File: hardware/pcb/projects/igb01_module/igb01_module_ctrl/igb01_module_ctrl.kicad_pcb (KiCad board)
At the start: 2 copper layers, 131 x 111 mm, 300 parts, among them J1 ST_JACK_MIDI_OUT, J10 JACK_MAIN_L_OUT, J11 JACK_MAIN_R_OUT, J12 ST_JACK_MIDI_IN, J13 JACK_RST_OUT, J14 JACK_CV_Y_IN, J15 JACK_CV_E_OUT, J16 JACK_CV_F_OUT, J17 JACK_CV_G_OUT, J18 JACK_CV_H_OUT, J19 JACK_RTN_L_IN, J2 JACK_CLK_OUT, J20 JACK_RTN_R_IN, J21 JACK_SND_L_OUT, J22 JACK_SND_R_OUT, J23 TYPE_SELECT, J24 LEFT_CON, J25 RIGHT_CON, J26 TYPE_SELECT, J27 SWD_CON, J28 DISP_CON1, J29 Micro_SD_Card, J3 JACK_CV_X_IN, J30 Conn_01x03, J31 Conn_01x03, J32 Conn_01x03, J33 POWER_CON, J4 JACK_CV_A_OUT, J5 JACK_CV_B_OUT, J6 JACK_CV_C_OUT, J7 JACK_CV_D_OUT, J8 JACK_EXT_L_IN, J9 JACK_EXT_R_IN, SW1 SW_Push_45deg, SW10 SW_Push_45deg, SW11 SW_Push_45deg, SW12 SW_Push_45deg, SW13 SW_Push_45deg, SW14 SW_Push_45deg, SW15 SW_Push_45deg, SW16 SW_Push_45deg, SW17 SW_Push_45deg, SW18 SW_Push_45deg, SW19 SW_Push_45deg, SW2 SW_Push_45deg, SW20 SW_Push_45deg, SW21 SW_Push_45deg, SW22 SW_Push_45deg, SW23 SW_Push_45deg, SW24 SW_Push_45deg, SW25 SW_Push_45deg, SW26 SW_Push_45deg, SW27 SW_Push_45deg, SW28 SW_Push_45deg, SW29 SW_Push_45deg, SW3 SW_Push_45deg, SW30 SW_Push_45deg, SW31 SW_Push_45deg, SW32 SW_Push_45deg, SW33 SW_Push_45deg, SW34 SW_Push_45deg, SW35 SW_Push_45deg, SW36 SW_Push_45deg, SW4 SW_Push_45deg, SW5 SW_Push_45deg, SW6 SW_Push_45deg, SW7 SW_Push_45deg, SW8 SW_Push_45deg, SW9 SW_Push_45deg, U1 TL074, U10 STM32G431RBTx, U11 TL074, U12 R-78B5.0-2.0, U13 LDK320-3.3V, U14 LDK320-3.3V, U15 LM4040DBZ-10, U2 TL074, U3 74AHCT1G125, U4 TLP2361, U5 74AHCT1G125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

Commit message: update igb01 module control board
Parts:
- removed the C41 at (291.0, 124.2)
- removed the C42 at (291.0, 129.2)
- removed the C43 at (291.0, 126.7)
- removed the C44 at (291.0, 131.7)
- removed the C45 at (291.0, 134.3)
- removed the C46 at (295.0, 101.6)
- removed the C47 at (291.0, 136.8)
- removed the C48 at (295.0, 104.1)
- removed the R19 at (299.0, 134.3)
- removed the R29 at (303.0, 121.7)
- removed the R32 at (303.0, 129.2)
- removed the R48 at (307.0, 106.6)
- added C26: 10u, Capacitor_SMD:C_0805_2012Metric, B.Cu at (115.5, 113.1)
- C1, C10, C11, C12, C13, C14, C15, C16, C17, C18, C19, C2, C20, C21, C22, C23, C24, C25, C3, C4, C5, C6, C7, C8, C9, FB1, FB2, FB3, J23, J26, J27, JP1, R11, R12, R13, R14, R15, R16, R17, R18, U1, U11, U12, U13, U14, U15, U2, U3, U4, U5, U6, U7, U8, U9, Y1: moved to B.Cu
- C27: renamed from C26; moved to B.Cu
- C28: renamed from C27; footprint Capacitor_SMD:C_1206_3216Metric -> Capacitor_SMD:C_0805_2012Metric; moved to B.Cu
- C29: renamed from C28; moved to B.Cu
- C30: renamed from C29; moved to B.Cu
- C31: renamed from C30; moved to B.Cu
- C32: renamed from C31; moved to B.Cu
- C33: renamed from C32; moved to B.Cu
- C34: renamed from C33; moved to B.Cu
- C35: renamed from C34; moved to B.Cu
- C36: renamed from C35; moved to B.Cu
- C37: renamed from C36; moved to B.Cu
- C38: renamed from C37; moved to B.Cu
- C39: renamed from C38; moved to B.Cu
- C40: renamed from C39; moved to B.Cu
- C41: renamed from C40; moved to B.Cu
- C42: renamed from C49; moved to B.Cu
- C43: renamed from C50; moved to B.Cu
- C44: renamed from C51; moved to B.Cu
- C45: renamed from C52; moved to B.Cu
- C46: renamed from C53; moved to B.Cu
- C47: renamed from C54; moved to B.Cu
- C48: renamed from C55; moved to B.Cu
- C49: renamed from C56; moved to B.Cu
- C50: renamed from C57; moved to B.Cu
- C51: renamed from C58; value 47u -> 100u; moved to B.Cu
- C52: renamed from C59; moved to B.Cu
- C53: renamed from C60; moved to B.Cu
- C54: renamed from C61; moved to B.Cu
- C55: renamed from C62; moved to B.Cu
- C56: renamed from C63; moved to B.Cu
- C57: renamed from C64; moved to B.Cu
- C58: renamed from C65; moved to B.Cu
- D1: footprint Diode_SMD:D_SOD-323_HandSoldering -> custom:SOD-123; moved to B.Cu
- D10, D11, D12, D13, D14, D15, D16, D17, D18, D19, D2, D20, D21, D22, D23, D24, D25, D26, D27, D28, D29, D3, D30, D31, D32, D33, D34, D35, D36, D37, D38, D39, D4, D40, D41, D5, D6, D7, D8, D9: footprint Diode_SMD:D_SOD-323_HandSoldering -> Diode_SMD:D_SOD-523; moved to B.Cu
- D42, D43: footprint Diode_SMD:D_SOD-123F -> custom:SOD-123; moved to B.Cu
- R1, R10, R5, R6: footprint Resistor_SMD:R_0603_1608Metric -> Resistor_SMD:R_1206_3216Metric; moved to B.Cu
- R19: renamed from R20; moved to B.Cu
- R2, R3, R4, R7, R8, R9: footprint Resistor_SMD:R_0603_1608Metric -> Resistor_SMD:R_0805_2012Metric; moved to B.Cu
- R20: renamed from R21; moved to B.Cu
- R21: renamed from R22; moved to B.Cu
- R22: renamed from R23; moved to B.Cu
- R23: renamed from R24; moved to B.Cu
- R24: renamed from R25; moved to B.Cu
- R25: renamed from R26; moved to B.Cu
- R26: renamed from R27; moved to B.Cu
- R27: renamed from R28; moved to B.Cu
- R28: renamed from R30; moved to B.Cu
- R29: renamed from R31; moved to B.Cu
- R30: renamed from R33; footprint Resistor_SMD:R_0402_1005Metric -> Resistor_SMD:R_0603_1608Metric; moved to B.Cu
- R31: renamed from R34; moved to B.Cu
- R32: renamed from R35; footprint Resistor_SMD:R_0402_1005Metric -> Resistor_SMD:R_0603_1608Metric; moved to B.Cu
- R33: renamed from R36; value 100k -> 200k; moved to B.Cu
- R34: renamed from R37; moved to B.Cu
- R35: renamed from R38; moved to B.Cu
- R36: renamed from R39; footprint Resistor_SMD:R_0402_1005Metric -> Resistor_SMD:R_0603_1608Metric; moved to B.Cu
- R37: renamed from R40; footprint Resistor_SMD:R_0402_1005Metric -> Resistor_SMD:R_0603_1608Metric; moved to B.Cu
- R38: renamed from R41; footprint Resistor_SMD:R_0402_1005Metric -> Resistor_SMD:R_0603_1608Metric; moved to B.Cu
- R39: renamed from R42; footprint Resistor_SMD:R_0402_1005Metric -> Resistor_SMD:R_0603_1608Metric; moved to B.Cu
- R40: renamed from R43; moved to B.Cu
- R41: renamed from R44; footprint Resistor_SMD:R_0402_1005Metric -> Resistor_SMD:R_0603_1608Metric; moved to B.Cu
- R42: renamed from R45; footprint Resistor_SMD:R_0402_1005Metric -> Resistor_SMD:R_0603_1608Metric; moved to B.Cu
- R43: renamed from R46; footprint Resistor_SMD:R_0402_1005Metric -> Resistor_SMD:R_0805_2012Metric; moved to B.Cu
- R44: renamed from R47; footprint Resistor_SMD:R_0402_1005Metric -> Resistor_SMD:R_0805_2012Metric; moved to B.Cu
- R45: renamed from R49; footprint Resistor_SMD:R_0402_1005Metric -> Resistor_SMD:R_0603_1608Metric; moved to B.Cu
- R46: renamed from R50; moved to B.Cu
- R47: renamed from R51; value 100k -> 200k; moved to B.Cu
- R48: renamed from R52; moved to B.Cu
- R49: renamed from R53; moved to B.Cu
- R50: renamed from R54; moved to B.Cu
- R51: renamed from R55; footprint Resistor_SMD:R_0402_1005Metric -> Resistor_SMD:R_0603_1608Metric; moved to B.Cu
- R52: renamed from R56; footprint Resistor_SMD:R_0402_1005Metric -> Resistor_SMD:R_0603_1608Metric; moved to B.Cu
- R53: renamed from R57; footprint Resistor_SMD:R_0402_1005Metric -> Resistor_SMD:R_0603_1608Metric; moved to B.Cu
- R54: renamed from R58; footprint Resistor_SMD:R_0402_1005Metric -> Resistor_SMD:R_0603_1608Metric; moved to B.Cu
- R55: renamed from R59; footprint Resistor_SMD:R_0402_1005Metric -> Resistor_SMD:R_0603_1608Metric; moved to B.Cu
- R56: renamed from R60; footprint Resistor_SMD:R_0402_1005Metric -> Resistor_SMD:R_0603_1608Metric; moved to B.Cu
- R57: renamed from R61; footprint Resistor_SMD:R_0402_1005Metric -> Resistor_SMD:R_0805_2012Metric; moved to B.Cu
- R58: renamed from R62; footprint Resistor_SMD:R_0402_1005Metric -> Resistor_SMD:R_0805_2012Metric; moved to B.Cu
- R59: renamed from R63; footprint Resistor_SMD:R_0402_1005Metric -> Resistor_SMD:R_0603_1608Metric; moved to B.Cu
- R60: renamed from R64; footprint Resistor_SMD:R_0402_1005Metric -> Resistor_SMD:R_0603_1608Metric; moved to B.Cu
- R61: renamed from R65; footprint Resistor_SMD:R_0402_1005Metric -> Resistor_SMD:R_0603_1608Metric; moved to B.Cu
- R62: renamed from R66; footprint Resistor_SMD:R_0402_1005Metric -> Resistor_SMD:R_0603_1608Metric; moved to B.Cu
- R63: renamed from R67; moved to B.Cu
- R64: renamed from R68; moved to B.Cu
- R65: renamed from R69; moved to B.Cu
- R66: renamed from R70; moved to B.Cu
- R67: renamed from R71; moved to B.Cu
- R68: renamed from R72; footprint Resistor_SMD:R_0402_1005Metric -> Resistor_SMD:R_0603_1608Metric; moved to B.Cu
- R69: renamed from R73; footprint Resistor_SMD:R_0402_1005Metric -> Resistor_SMD:R_0603_1608Metric; moved to B.Cu
- R70: renamed from R74; footprint Resistor_SMD:R_0402_1005Metric -> Resistor_SMD:R_0805_2012Metric; moved to B.Cu
- R71: renamed from R75; footprint Resistor_SMD:R_0402_1005Metric -> Resistor_SMD:R_0805_2012Metric; moved to B.Cu
- R72: renamed from R76; footprint Resistor_SMD:R_0402_1005Metric -> Resistor_SMD:R_0603_1608Metric; moved to B.Cu
- R73: renamed from R77; footprint Resistor_SMD:R_0402_1005Metric -> Resistor_SMD:R_0603_1608Metric; moved to B.Cu
- R74: renamed from R78; footprint Resistor_SMD:R_0402_1005Metric -> Resistor_SMD:R_0603_1608Metric; moved to B.Cu
- R75: renamed from R79; footprint Resistor_SMD:R_0402_1005Metric -> Resistor_SMD:R_0603_1608Metric; moved to B.Cu
- R76: renamed from R80; moved to B.Cu
- R77: renamed from R81; moved to B.Cu
- R78: renamed from R82; moved to B.Cu
- R79: renamed from R83; moved to B.Cu
- R80: renamed from R84; footprint Resistor_SMD:R_0402_1005Metric -> Resistor_SMD:R_0603_1608Metric; moved to B.Cu
- R81: renamed from R85; footprint Resistor_SMD:R_0402_1005Metric -> Resistor_SMD:R_0603_1608Metric; moved to B.Cu
- R82: renamed from R86; moved to B.Cu
- R83: renamed from R87; footprint Resistor_SMD:R_0402_1005Metric -> Resistor_SMD:R_0805_2012Metric; moved to B.Cu
- R84: renamed from R88; footprint Resistor_SMD:R_0402_1005Metric -> Resistor_SMD:R_0805_2012Metric; moved to B.Cu
- R85: renamed from R89; moved to B.Cu
- R86: renamed from R90; moved to B.Cu
- R87: renamed from R91; moved to B.Cu
- R88: renamed from R92; moved to B.Cu
- moved J31 273.0 mm to (65.5, 155.0)
- moved FB2 267.4 mm to (60.2, 130.8)
- moved FB3 256.5 mm to (66.3, 112.0)
- moved FB1 255.0 mm to (66.3, 96.0)
- moved R10 250.8 mm to (52.5, 65.6), turned to -90 degrees
- moved U12 249.3 mm to (66.6, 129.4)
- moved R5 248.4 mm to (58.7, 60.3), turned to -90 degrees
- moved R1 247.7 mm to (58.7, 52.3), turned to -90 degrees
- moved D28 247.3 mm to (63.2, 82.0), turned to -90 degrees
- moved D32 246.8 mm to (57.5, 134.3)
- moved D29 246.6 mm to (61.2, 96.0), turned to -90 degrees
- moved D33 246.4 mm to (57.5, 148.3)
- moved D30 244.9 mm to (61.2, 110.0), turned to -90 degrees
- moved U4 244.8 mm to (71.5, 87.3), turned to -90 degrees
- moved D43 244.4 mm to (71.0, 112.9)
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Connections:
- R37 pad 2: /CV_A_OUT -> /CV_B_OUT
- R39 pad 2: /CV_B_OUT -> /CV_F_OUT
- R43 pad 2: /CV_A_OUT -> /CV_B_OUT
- R44 pad 2: /CV_B_OUT -> /CV_F_OUT
- R52 pad 2: /CV_C_OUT -> /CV_E_OUT
- R54 pad 2: /CV_D_OUT -> /CV_A_OUT
- R57 pad 2: /CV_C_OUT -> /CV_E_OUT
- R58 pad 2: /CV_D_OUT -> /CV_A_OUT
- R60 pad 2: /CV_E_OUT -> /CV_D_OUT
- R62 pad 2: /CV_F_OUT -> /CV_H_OUT
- R70 pad 2: /CV_E_OUT -> /CV_D_OUT
- R71 pad 2: /CV_F_OUT -> /CV_H_OUT
- R75 pad 2: /CV_H_OUT -> /CV_C_OUT
- R84 pad 2: /CV_H_OUT -> /CV_C_OUT
- U3 pad 4: Net-(R19-Pad2) -> /CLOCK_OUT
- U6 pad 4: Net-(R29-Pad2) -> /RESET_OUT
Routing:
- net /MIDI_OUT_TIP: track 0.00 -> 32.2 mm
- net /GPIO_CLOCK_OUT: track 0.00 -> 29.1 mm
- net /CORE_UART8_TX: track 0.00 -> 27.3 mm
- net /MIDI_OUT_RING: track 0.00 -> 26.7 mm
- net /MIDI_IN_VCC: track 0.00 -> 23.8 mm
- net /GPIO_RESET_OUT: track 0.00 -> 14.5 mm
- net +5V: track 0.00 -> 11.0 mm
- net Net-(J26-Pin_2): track 0.00 -> 10.5 mm
- net /CORE_SPI2_MOSI: track 0.00 -> 10.4 mm
- net /CORE_SPI2_CS_GPIO: track 0.00 -> 9.71 mm, vias 0 -> 1
- net Net-(D1-A): track 0.00 -> 9.20 mm
- net /MIDI_IN: track 0.00 -> 8.35 mm
- net Net-(D1-K): track 0.00 -> 7.82 mm
- net Net-(J1-TIP): track 0.00 -> 3.31 mm
- net Net-(J1-RING): track 0.00 -> 3.22 mm
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
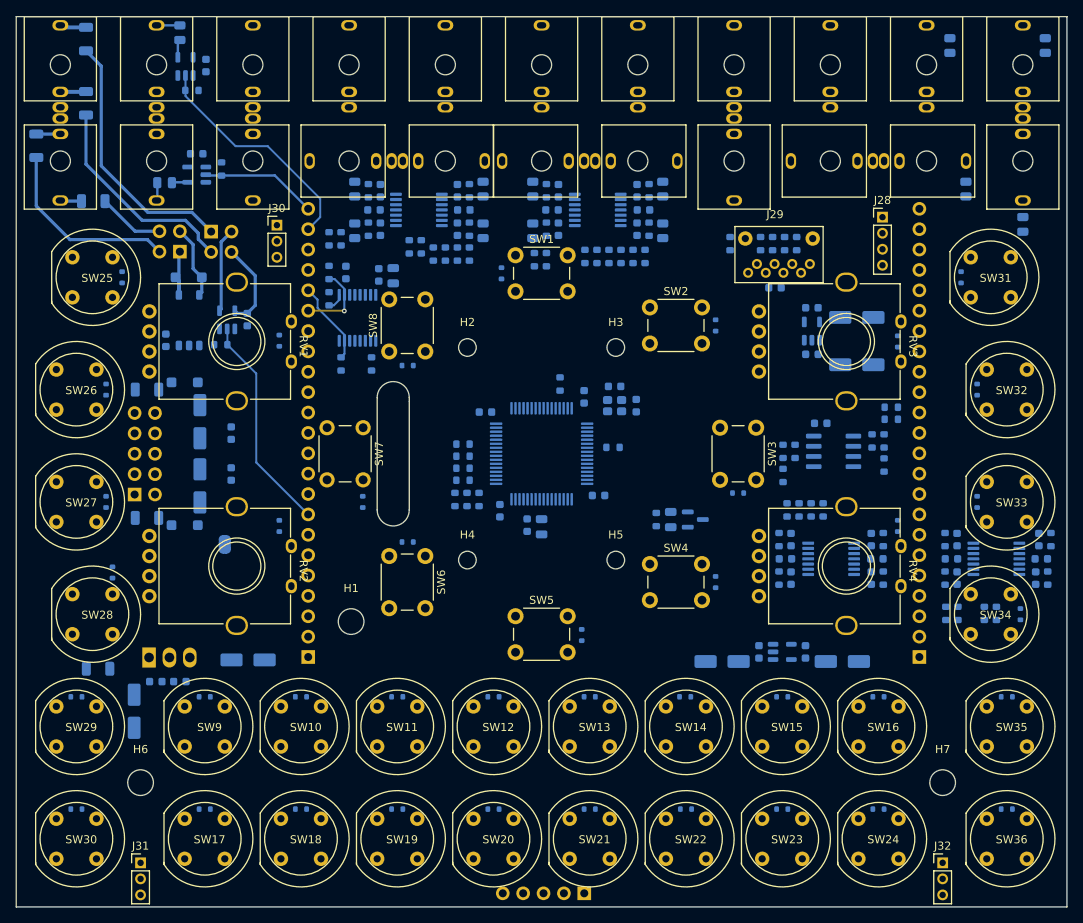
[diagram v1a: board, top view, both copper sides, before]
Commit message: update igb01 module control board: layout all nets
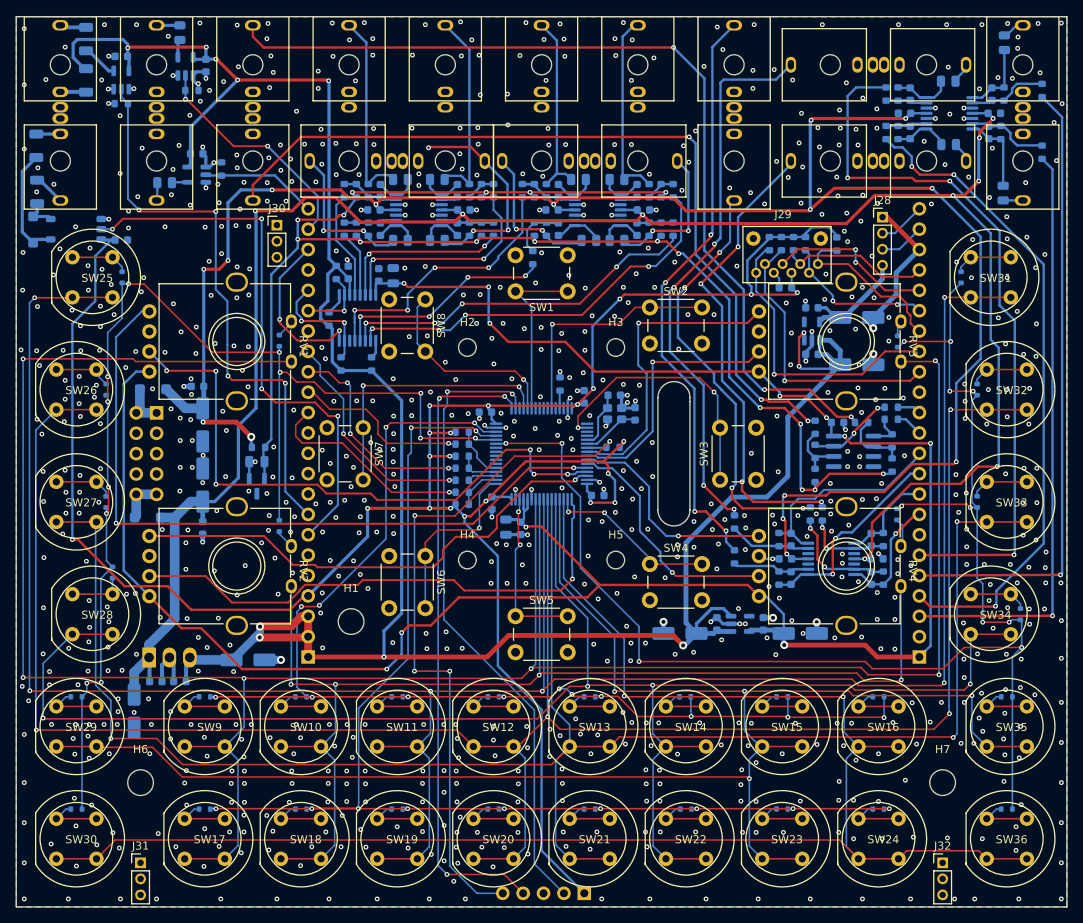
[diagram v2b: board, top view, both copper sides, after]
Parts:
- removed the D2 at (110.5, 81.5)
- removed the D3 at (137.2, 88.0)
- removed the D4 at (140.0, 108.9)
- removed the D5 at (137.2, 120.0)
- removed the D6 at (120.5, 126.6)
- removed the D7 at (98.8, 115.0)
- removed the D8 at (93.2, 110.0)
- removed the D9 at (98.8, 93.0)
- removed FB1, FB3: FerriteBead_Small, Resistor_SMD:R_1206_3216Metric
- removed FB2: FerriteBead, Resistor_SMD:R_1206_3216Metric
- removed J23, J26: TYPE_SELECT, Connector_PinSocket_2.54mm:PinSocket_2x02_P2.54mm_Vertical
- removed JP1: SolderJumper_2_Bridged, custom:GND_JUMPER_no_silk
- moved R17 66.3 mm to (177.9, 58.7)
- moved R27 65.9 mm to (158.4, 59.1), turned to 90 degrees
- moved R26 60.6 mm to (158.4, 64.0)
- moved R18 57.8 mm to (177.9, 66.4)
- moved C15 55.9 mm to (161.4, 59.1)
- moved R23 55.9 mm to (159.9, 59.1)
- moved C14 55.9 mm to (161.4, 64.0)
- moved C7 55.9 mm to (171.9, 61.5)
- moved R22 55.9 mm to (159.9, 64.0)
- moved C5 55.9 mm to (171.7, 59.1)
- moved R13 55.9 mm to (173.2, 59.1)
- moved C6 55.9 mm to (171.2, 64.0)
- moved C9 55.9 mm to (160.8, 61.5)
- moved R14 55.9 mm to (172.8, 64.0)
- moved U2 55.9 mm to (166.3, 61.5)
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- renumbered D18 to D10, D19 to D11, D20 to D12, D21 to D13, D22 to D14, D23 to D15, D24 to D16, D25 to D17, D26 to D18, D27 to D19, D10 to D2, D28 to D20, D29 to D21, D30 to D22, D31 to D23, D32 to D24, D33 to D25, D34 to D26, D35 to D27, D36 to D28, D37 to D29, D11 to D3, D38 to D30, D39 to D31, D40 to D32, D41 to D33, D42 to D34, D43 to D35, D12 to D4, D13 to D5, D14 to D6, D15 to D7, D16 to D8, D17 to D9
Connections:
- C10 pad 1: GNDA -> GND
- C12 pad 2: /IN2L -> /IN2R
- C13 pad 2: /IN2R -> /IN2L
- C14 pad 2: /MAIN_L_OUT -> /SND_L_OUT
- C15 pad 2: /MAIN_R_OUT -> /MAIN_L_OUT
- C16 pad 2: GNDA -> GND
- C17 pad 2: GNDA -> GND
- C18 pad 1: GNDA -> GND
- C2 pad 2: GNDA -> GND
- C25 pad 2: GNDA -> GND
- C26 pad 2: GNDA -> GND
- C27 pad 1: GNDA -> GND
- C28 pad 2: GNDA -> GND
- C29 pad 1: GNDA -> GND
- C3 pad 2: /IN1L -> /IN1R
- C31 pad 2: GNDA -> GND
- C38 pad 1: GNDA -> GND
- C39 pad 2: GNDA -> GND
- C4 pad 2: /IN1R -> /IN1L
- C44 pad 1: Net-(U12-IN) -> +12V
- C45 pad 1: Net-(U12-IN) -> +12V
- C5 pad 2: /SND_L_OUT -> /MAIN_R_OUT
- C52 pad 2: GNDA -> GND
- C53 pad 2: GNDA -> GND
- C54 pad 2: GNDA -> GND
- C55 pad 2: GNDA -> GND
- C56 pad 2: GNDA -> GND
- C7 pad 2: GNDA -> GND
- C8 pad 2: GNDA -> GND
- C9 pad 1: GNDA -> GND
- D1 pad 1: Net-(D1-K) -> /MIDI_IN_VCC
- D1 pad 2: Net-(D1-A) -> /MIDI_IN
- D10 pad 2: /BTN_MUX_C -> /BTN_MUX_B
- D11 pad 2: /BTN_MUX_C -> /BTN_MUX_B
- D12 pad 2: /BTN_MUX_C -> /BTN_MUX_B
- D13 pad 2: /BTN_MUX_C -> /BTN_MUX_B
- D14 pad 2: /BTN_MUX_C -> /BTN_MUX_B
- D15 pad 2: /BTN_MUX_C -> /BTN_MUX_B
- D16 pad 2: /BTN_MUX_C -> /BTN_MUX_B
- D17 pad 2: /BTN_MUX_C -> /BTN_MUX_B
- D18 pad 2: /BTN_MUX_D -> /BTN_MUX_C
- D19 pad 2: /BTN_MUX_D -> /BTN_MUX_C
- D2 pad 2: /BTN_MUX_B -> /BTN_MUX_A
- D20 pad 2: /BTN_MUX_D -> /BTN_MUX_C
- D21 pad 2: /BTN_MUX_D -> /BTN_MUX_C
- D22 pad 2: /BTN_MUX_D -> /BTN_MUX_C
- D23 pad 2: /BTN_MUX_D -> /BTN_MUX_C
- D24 pad 2: /BTN_MUX_D -> /BTN_MUX_C
- D25 pad 2: /BTN_MUX_D -> /BTN_MUX_C
- D26 pad 2: /BTN_MUX_E -> /BTN_MUX_D
- D27 pad 2: /BTN_MUX_E -> /BTN_MUX_D
- D28 pad 2: /BTN_MUX_E -> /BTN_MUX_D
- D29 pad 2: /BTN_MUX_E -> /BTN_MUX_D
- D3 pad 2: /BTN_MUX_B -> /BTN_MUX_A
- D30 pad 2: /BTN_MUX_E -> /BTN_MUX_D
- D31 pad 2: /BTN_MUX_E -> /BTN_MUX_D
- D32 pad 2: /BTN_MUX_E -> /BTN_MUX_D
- D33 pad 2: /BTN_MUX_E -> /BTN_MUX_D
- D34 pad 2: Net-(D42-A) -> Net-(D34-A)
- D35 pad 1: Net-(D43-K) -> Net-(D35-K)
- D4 pad 2: /BTN_MUX_B -> /BTN_MUX_A
- D5 pad 2: /BTN_MUX_B -> /BTN_MUX_A
- D6 pad 2: /BTN_MUX_B -> /BTN_MUX_A
- D7 pad 2: /BTN_MUX_B -> /BTN_MUX_A
- D8 pad 2: /BTN_MUX_B -> /BTN_MUX_A
- D9 pad 2: /BTN_MUX_B -> /BTN_MUX_A
- J10 pad 1: GNDA -> GND
- J11 pad 1: GNDA -> GND
- J14 pad 1: GNDA -> GND
- J14 pad 2: GNDA -> GND
- J15 pad 1: GNDA -> GND
- J16 pad 1: GNDA -> GND
- J17 pad 1: GNDA -> GND
- J18 pad 1: GNDA -> GND
- J19 pad 1: GNDA -> GND
- J19 pad 2: GNDA -> GND
- J20 pad 1: GNDA -> GND
- J20 pad 2: GNDA -> GND
- J21 pad 1: GNDA -> GND
- J22 pad 1: GNDA -> GND
- J25 pad 2: GNDA -> GND
- J25 pad 7: GNDA -> GND
- J3 pad 1: GNDA -> GND
- J3 pad 2: GNDA -> GND
- J33 pad 1: Net-(J33-Pin_1) -> Net-(D35-K)
- J33 pad 10: Net-(J33-Pin_10) -> Net-(D34-A)
- J33 pad 2: Net-(J33-Pin_1) -> Net-(D35-K)
- J33 pad 9: Net-(J33-Pin_10) -> Net-(D34-A)
- J4 pad 1: GNDA -> GND
- J5 pad 1: GNDA -> GND
- J6 pad 1: GNDA -> GND
- J7 pad 1: GNDA -> GND
- J8 pad 1: GNDA -> GND
- J8 pad 2: GNDA -> GND
- J9 pad 1: GNDA -> GND
- J9 pad 2: GNDA -> GND
- R11 pad 1: /IN1L -> /IN1R
- R12 pad 1: /IN1R -> /IN1L
- R13 pad 1: /SND_L_OUT -> /MAIN_R_OUT
- R15 pad 2: /RTN_L_IN -> /RTN_R_IN
- R16 pad 2: /RTN_R_IN -> /RTN_L_IN
- R17 pad 2: /OUT1L -> /OUT1R
- R18 pad 2: /OUT1R -> /OUT2R
- R20 pad 1: /IN2L -> /IN2R
- R21 pad 1: /IN2R -> /IN2L
- R22 pad 1: /MAIN_L_OUT -> /SND_L_OUT
- R23 pad 1: /MAIN_R_OUT -> /MAIN_L_OUT
- R24 pad 2: /EXT_L_IN -> /EXT_R_IN
- R25 pad 2: /EXT_R_IN -> /EXT_L_IN
- R27 pad 2: /OUT2R -> /OUT1L
- R41 pad 1: /DAC_OUT_A -> /DAC_OUT_G
- R42 pad 1: /DAC_OUT_B -> /DAC_OUT_E
- R5 pad 2: /MIDI_OUT_RING -> +5V
- R56 pad 1: /DAC_OUT_D -> /DAC_OUT_A
- R68 pad 1: /DAC_OUT_E -> /DAC_OUT_H
- R80 pad 1: /DAC_OUT_G -> /DAC_OUT_D
- R81 pad 1: /DAC_OUT_H -> /DAC_OUT_B
- RV1 pad 2: GNDA -> GND
- RV2 pad 2: GNDA -> GND
- RV3 pad 2: GNDA -> GND
- RV4 pad 2: GNDA -> GND
- SW1 pad 1: Net-(D2-K) (its old number) -> /C_BTN_1
- SW1 pad 2: /BTN_MUX_1 -> GND
- SW2 pad 1: Net-(D3-K) (its old number) -> /C_BTN_2
- SW2 pad 2: /BTN_MUX_2 -> GND
- SW3 pad 1: Net-(D4-K) (its old number) -> /C_BTN_3
- SW3 pad 2: /BTN_MUX_3 -> GND
- SW4 pad 1: Net-(D5-K) (its old number) -> /C_BTN_4
- SW4 pad 2: /BTN_MUX_4 -> GND
- SW5 pad 1: Net-(D6-K) (its old number) -> /C_BTN_5
- SW5 pad 2: /BTN_MUX_5 -> GND
- SW6 pad 1: Net-(D7-K) (its old number) -> /C_BTN_6
- SW6 pad 2: /BTN_MUX_6 -> GND
- SW7 pad 1: Net-(D8-K) (its old number) -> /C_BTN_7
- SW7 pad 2: /BTN_MUX_7 -> GND
- SW8 pad 1: Net-(D9-K) (its old number) -> /C_BTN_8
- SW8 pad 2: /BTN_MUX_8 -> GND
- U1 pad 1: /IN1L -> /IN1R
- U1 pad 10: GNDA -> GND
- U1 pad 12: GNDA -> GND
- U1 pad 14: /IN2L -> /IN2R
- U1 pad 3: GNDA -> GND
- U1 pad 5: GNDA -> GND
- U1 pad 7: /IN1R -> /IN1L
- U1 pad 8: /IN2R -> /IN2L
- U10 pad 18: unconnected-(U10-PA4-Pad18) -> /C_BTN_4
- U10 pad 19: unconnected-(U10-PA5-Pad19) -> /BTN_MUX_8
- U10 pad 2: unconnected-(U10-PC13-Pad2) -> /C_BTN_3
- U10 pad 20: unconnected-(U10-PA6-Pad20) -> /BTN_MUX_7
- U10 pad 21: unconnected-(U10-PA7-Pad21) -> /BTN_MUX_6
- U10 pad 22: /BTN_MUX_1 -> /BTN_MUX_5
- U10 pad 23: /BTN_MUX_2 -> /BTN_MUX_4
- U10 pad 24: unconnected-(U10-PB0-Pad24) -> /BTN_MUX_3
- U10 pad 25: unconnected-(U10-PB1-Pad25) -> /BTN_MUX_2
- U10 pad 26: unconnected-(U10-PB2-Pad26) -> /BTN_MUX_1
- U10 pad 27: GNDA -> GND
- U10 pad 30: unconnected-(U10-PB10-Pad30) -> /C_BTN_5
- U10 pad 33: unconnected-(U10-PB11-Pad33) -> /C_BTN_6
- U10 pad 38: /BTN_MUX_3 -> unconnected-(U10-PC6-Pad38)
- U10 pad 39: /BTN_MUX_4 -> unconnected-(U10-PC7-Pad39)
- U10 pad 40: /BTN_MUX_5 -> unconnected-(U10-PC8-Pad40)
- U10 pad 41: /BTN_MUX_6 -> unconnected-(U10-PC9-Pad41)
- U10 pad 43: unconnected-(U10-PA9-Pad43) -> /BTN_MUX_D
- U10 pad 44: unconnected-(U10-PA10-Pad44) -> /BTN_MUX_C
- U10 pad 45: unconnected-(U10-PA11-Pad45) -> /BTN_MUX_B
- U10 pad 46: unconnected-(U10-PA12-Pad46) -> /BTN_MUX_A
- U10 pad 52: /BTN_MUX_7 -> /C_BTN_7
- U10 pad 53: /BTN_MUX_8 -> /C_BTN_8
- U10 pad 54: unconnected-(U10-PC12-Pad54) -> /C_BTN_1
- U10 pad 56: /BTN_MUX_A -> unconnected-(U10-PB3-Pad56)
- U10 pad 57: /BTN_MUX_B -> unconnected-(U10-PB4-Pad57)
- U10 pad 58: /BTN_MUX_C -> unconnected-(U10-PB5-Pad58)
- U10 pad 59: /BTN_MUX_D -> /C_BTN_2
- U10 pad 60: /BTN_MUX_E -> unconnected-(U10-PB7-Pad60)
- U11 pad 10: GNDA -> GND
- U11 pad 12: GNDA -> GND
- U11 pad 3: GNDA -> GND
- U11 pad 5: GNDA -> GND
- U12 pad 1: Net-(U12-IN) -> +12V
- U14 pad 2: GNDA -> GND
- U15 pad 1: GNDA -> GND
- U2 pad 1: /SND_L_OUT -> /MAIN_R_OUT
- U2 pad 10: GNDA -> GND
- U2 pad 12: GNDA -> GND
- U2 pad 14: /MAIN_R_OUT -> /MAIN_L_OUT
- U2 pad 3: GNDA -> GND
- U2 pad 5: GNDA -> GND
- U2 pad 8: /MAIN_L_OUT -> /SND_L_OUT
- U4 pad 1: Net-(D1-K) -> /MIDI_IN_VCC
- U4 pad 3: Net-(D1-A) -> /MIDI_IN
- U5 pad 4: Net-(J26-Pin_2) -> /MIDI_OUT_TIP
- U7 pad 3: GNDA -> GND
- U7 pad 4: GNDA -> GND
- U7 pad 5: GNDA -> GND
- U8 pad 14: GNDA -> GND
- U9 pad 10: GNDA -> GND
- U9 pad 12: GNDA -> GND
- U9 pad 3: GNDA -> GND
- U9 pad 5: GNDA -> GND
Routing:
- net +3.3V: track 0.00 -> 295.3 mm, vias 0 -> 21
- net /BTN_MUX_1: track 0.00 -> 288.4 mm, vias 0 -> 6
- net +5V: track 11.0 -> 298.9 mm, vias 0 -> 11
- net /BTN_MUX_3: track 0.00 -> 287.2 mm, vias 0 -> 6
- net +3.3VA: track 0.00 -> 276.7 mm, vias 0 -> 11
- net /BTN_MUX_4: track 0.00 -> 258.0 mm, vias 0 -> 4
- net +12V: track 0.00 -> 251.1 mm, vias 0 -> 9
- net -12V: track 0.00 -> 238.3 mm, vias 0 -> 15
- net /BTN_MUX_5: track 0.00 -> 228.6 mm, vias 0 -> 3
- net /BTN_MUX_8: track 0.00 -> 206.2 mm, vias 0 -> 2
- net /BTN_MUX_6: track 0.00 -> 204.7 mm, vias 0 -> 4
- net /BTN_MUX_7: track 0.00 -> 204.7 mm, vias 0 -> 4
- net /VREF_-10V: track 0.00 -> 188.5 mm, vias 0 -> 17
- net /BTN_MUX_D: track 0.00 -> 181.7 mm, vias 0 -> 12
- net /BTN_MUX_2: track 0.00 -> 157.2 mm, vias 0 -> 4
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- added copper zone on B.Cu, net GND
- added copper zone on F.Cu, net GND
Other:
- outline, holes or cut-outs redrawn

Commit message: igb01 module control board ver 0.1
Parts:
- added J23: JTAG, Connector_PinHeader_1.27mm:PinHeader_2x05_P1.27mm_Vertical, B.Cu at (106.0, 158.8)
- H1, H6, H7: footprint MountingHole:MountingHole_3.2mm_M3 -> custom:MountingHole_3.2mm_M3_mod
- H2, H3, H4, H5: footprint MountingHole:MountingHole_2.2mm_M2 -> custom:MountingHole_2.2mm_M2_mod
- J27: footprint Connector_PinHeader_2.54mm:PinHeader_1x05_P2.54mm_Vertical -> Connector_PinSocket_2.54mm:PinSocket_1x05_P2.54mm_Vertical
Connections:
- net /SWCLK renamed /JTCK-SWCLK
- net /SWDIO renamed /JTMS-SWDIO
- U10 pad 51: unconnected-(U10-PA15-Pad51) -> /JTDI
- U10 pad 56: unconnected-(U10-PB3-Pad56) -> /JTDO-TRACESWO
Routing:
- net /JTDO-TRACESWO: track 0.00 -> 79.4 mm, vias 0 -> 2
- net /JTDI: track 0.00 -> 75.9 mm, vias 0 -> 2
- net +3.3V: track 295.3 -> 314.7 mm
- net /JTCK-SWCLK: track 79.1 -> 90.9 mm, vias 2 -> 3
- net /CV_F_OUT: track 26.5 -> 18.5 mm, vias 3 -> 2
- net /~{MCU_RESET}: track 87.3 -> 91.6 mm, vias 4 -> 5
- net /JTMS-SWDIO: track 79.8 -> 83.7 mm, vias 3 -> 2
- net /C_BTN_7: track 34.1 -> 36.8 mm
- net /OUT2R: track 74.1 -> 73.0 mm
- net -12V: track 238.3 -> 237.5 mm
- net +12V: track 251.1 -> 251.9 mm
- net /C_BTN_8: track 24.8 -> 25.5 mm
- net /OUT1R: track 78.3 -> 77.7 mm
- net GND: vias 891 -> 1024
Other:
- board size 131 x 111 mm -> 131 x 111.1 mm
- board text added: "3V3"
- board text added: "CLK"
- board text added: "Designed by centrevillage"
- board text added: "GND"
- board text added: "IGB01 Module Control Ver 0.1"
- board text added: "IO"
- board text added: "MINI-JTAG"
- board text added: "NRST"
- board text added: "SWD"
